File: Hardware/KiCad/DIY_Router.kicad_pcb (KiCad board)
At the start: 4 copper layers, 90 parts, among them IC1 HLK-7628N, IC2 TPS62A06ADRLR, J1 2171790001, J10 2041262-1, J2 RJ45_Hanrun_HR911105A_Horizon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, J3 RJ45_Hanrun_HR911105A_Horizon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, J4 RJ45_Hanrun_HR911105A_Horizon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, J5 Conn_01x06_Pin, J6 Conn_02x07_Odd_Even, J7 RJ45_Hanrun_HR911105A_Horizon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, J8 USB_A, J9 SIM8066-6-1-14-01-A, SW1 436333033816, SW2 436333033816, SW3 450405020524, U1 XR22801IL32TR-F, U2 USBLC6-2SC6Y, U3 USBLC6-2SC6Y, U4 USB2422T/MJ, U5 EMIF03-SIM02M8, Y1 ABM8-25.000MHZ-B2-T3, Y2 ABM8-24.000MHZ-B2-T

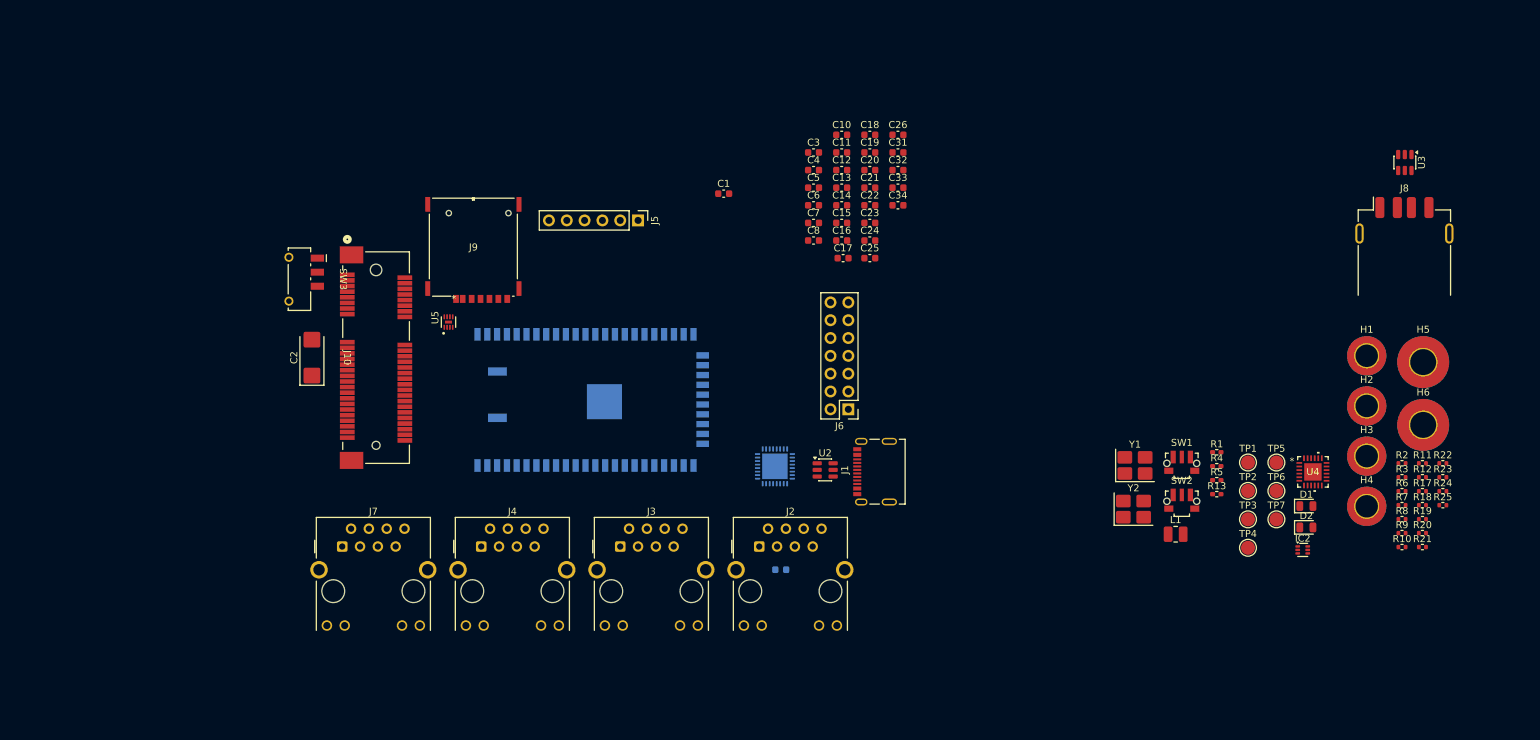
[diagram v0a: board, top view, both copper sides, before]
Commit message: Layout: Get started on PCB layout
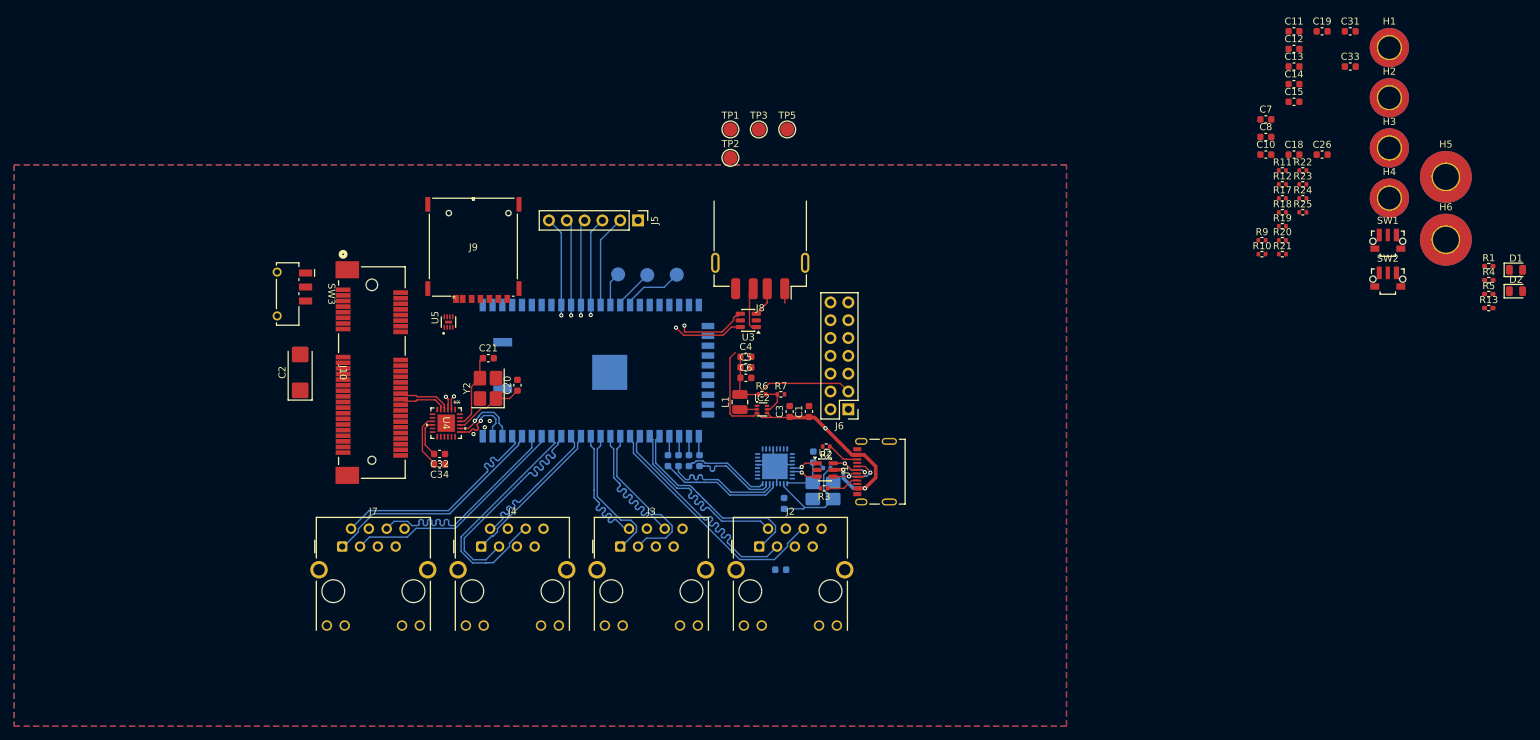
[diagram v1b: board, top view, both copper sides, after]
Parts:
- C16, C17, C22, C23, C24, C25, R8, TP4, TP6, TP7, Y1: moved to B.Cu
- moved U4 123.7 mm to (111.6, 86.8), turned to -90 degrees
- moved TP4 97.9 mm to (136.1, 65.6), turned to 180 degrees
- moved U3 96.2 mm to (154.7, 72.2), turned to 180 degrees
- moved TP6 94.8 mm to (140.2, 65.7), turned to 180 degrees
- moved Y2 93.6 mm to (117.5, 81.8), turned to 90 degrees
- moved TP7 92.3 mm to (144.4, 65.7), turned to 180 degrees
- moved R6 92.3 mm to (156.6, 82.7)
- moved J8 91.9 mm to (156.3, 60.4), turned to 180 degrees
- moved R7 89.9 mm to (159.3, 82.7)
- moved TP3 89.2 mm to (156.2, 45.0)
- moved TP1 87.7 mm to (152.1, 45.0)
- moved TP2 87.7 mm to (152.1, 49.0)
- moved TP5 84.3 mm to (160.2, 45.0)
- moved R3 82.4 mm to (165.4, 96.1), turned to 180 degrees
- moved R8 82.3 mm to (165.8, 93.2), turned to 180 degrees
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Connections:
- net MDI_RN_P0 renamed MDI_P0_RN
- net MDI_RN_P1 renamed MDI_P1_RN
- net MDI_RN_P2 renamed MDI_P2_RN
- net MDI_RN_P3 renamed MDI_P3_RN
- net MDI_RN_P4 renamed MDI_P4_RN
- net MDI_RP_P0 renamed MDI_P0_RP
- net MDI_RP_P1 renamed MDI_P1_RP
- net MDI_RP_P2 renamed MDI_P2_RP
- net MDI_RP_P3 renamed MDI_P3_RP
- net MDI_RP_P4 renamed MDI_P4_RP
- net MDI_TN_P0 renamed MDI_P0_TN
- net MDI_TN_P1 renamed MDI_P1_TN
- net MDI_TN_P2 renamed MDI_P2_TN
- net MDI_TN_P3 renamed MDI_P3_TN
- net MDI_TN_P4 renamed MDI_P4_TN
- net MDI_TP_P0 renamed MDI_P0_TP
- net MDI_TP_P1 renamed MDI_P1_TP
- net MDI_TP_P2 renamed MDI_P2_TP
- net MDI_TP_P3 renamed MDI_P3_TP
- net MDI_TP_P4 renamed MDI_P4_TP
- J1 pad A1B12: Net-(J1-CC2) -> GND
- J1 pad B1A12: Net-(J1-CC2) -> GND
- J1 pad SH1: Net-(J1-CC2) -> GND
- J1 pad SH2: Net-(J1-CC2) -> GND
- J1 pad SH3: Net-(J1-CC2) -> GND
- J1 pad SH4: Net-(J1-CC2) -> GND
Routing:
- net EPHY_LED4: track 0.00 -> 71.3 mm, vias 0 -> 1
- net EPHY_LED1: track 0.00 -> 68.5 mm, vias 0 -> 1
- net EPHY_LED3: track 0.00 -> 63.2 mm, vias 0 -> 1
- net EPHY_LED2: track 0.00 -> 60.4 mm, vias 0 -> 1
- net VBUS: track 0.00 -> 53.9 mm, vias 0 -> 3
- net /USB_HUB/USB_OUT_DN: track 0.00 -> 53.1 mm, vias 0 -> 2
- net /USB_HUB/USB_OUT_DP: track 0.00 -> 53.0 mm, vias 0 -> 2
- net MDI_P1_RN: track 0.00 -> 35.2 mm
- net MDI_P1_RP: track 0.00 -> 35.0 mm
- net MDI_P3_RN: track 0.00 -> 34.3 mm
- net MDI_P3_RP: track 0.00 -> 34.1 mm
- net MDI_P4_RP: track 0.00 -> 32.9 mm
- net MDI_P4_TP: track 0.00 -> 32.8 mm
- net MDI_P4_TN: track 0.00 -> 32.7 mm
- net MDI_P4_RN: track 0.00 -> 32.7 mm
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- added copper zone on B.Cu, net GND
- added copper zone on F.Cu, net GND
- added copper zone on In2.Cu, net GND

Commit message: Hardware: Lay out and route GPIO Header, USB and some other stuff
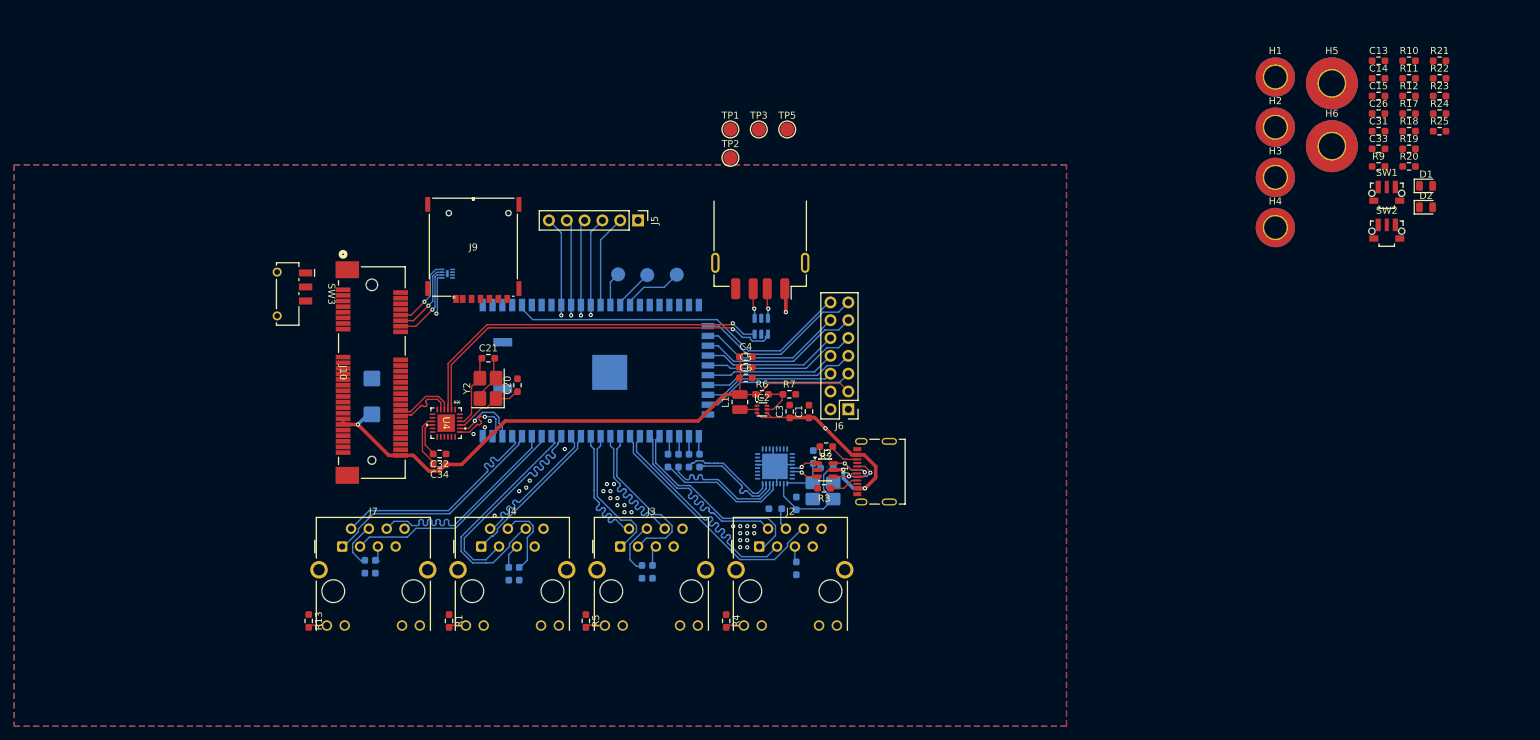
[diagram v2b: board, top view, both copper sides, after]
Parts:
- C1, C13, C14, C15, C16, C17, C20, C21, C22, C23, C24, C25, C26, C3, C31, C32, C33, C34, C4, C5, C6, C9: footprint Capacitor_SMD:C_0603_1608Metric -> Resistor_SMD:R_0603_1608Metric_Pad0.98x0.95mm_HandSolder
- C10, C11, C12, C18, C19, C7, C8: footprint Capacitor_SMD:C_0603_1608Metric -> Resistor_SMD:R_0603_1608Metric_Pad0.98x0.95mm_HandSolder; moved to B.Cu
- C2, U3, U5: moved to B.Cu
- R1, R13, R4, R5: footprint Resistor_SMD:R_0402_1005Metric_Pad0.72x0.64mm_HandSolder -> Resistor_SMD:R_0603_1608Metric_Pad0.98x0.95mm_HandSolder
- R10, R11, R12, R17, R18, R19, R2, R20, R21, R22, R23, R24, R25, R3, R6, R7, R8, R9: footprint Resistor_SMD:R_0402_1005Metric -> Resistor_SMD:R_0603_1608Metric_Pad0.98x0.95mm_HandSolder
- moved R13 174.0 mm to (92.0, 115.0), turned to -90 degrees
- moved R1 156.6 mm to (112.0, 115.0), turned to -90 degrees
- moved C19 155.0 mm to (101.5, 107.3), turned to -90 degrees
- moved C18 144.9 mm to (100.0, 107.3), turned to -90 degrees
- moved R5 136.9 mm to (131.5, 115.0), turned to -90 degrees
- moved C8 124.6 mm to (120.5, 108.3), turned to -90 degrees
- moved C7 124.6 mm to (122.0, 108.3), turned to -90 degrees
- moved C11 120.7 mm to (139.5, 108.0), turned to -90 degrees
- moved R4 119.0 mm to (151.5, 115.0), turned to -90 degrees
- moved C12 117.9 mm to (141.0, 108.0), turned to -90 degrees
- moved C10 89.2 mm to (161.5, 107.5), turned to -90 degrees
- moved R21 35.5 mm to (253.2, 35.2)
- moved R10 34.6 mm to (248.8, 35.2)
- moved R22 23.5 mm to (253.2, 37.7)
- moved R23 23.2 mm to (253.2, 40.2)
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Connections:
- J6 pad 11: /DIY_Router/I2C_SCL -> /DIY_Router/SPI_CS1
- J6 pad 12: /DIY_Router/SPI_CS1 -> /DIY_Router/I2C_SDA
- J6 pad 13: /DIY_Router/I2C_SDA -> /DIY_Router/I2C_SCL
- J6 pad 6: /DIY_Router/SPI_MOSI -> UART_TXD0
- J6 pad 7: UART_TXD0 -> /DIY_Router/GPIO0
- J6 pad 8: /DIY_Router/SPI_MISO -> /DIY_Router/SPI_MOSI
- J6 pad 9: /DIY_Router/GPIO0 -> /DIY_Router/SPI_MISO
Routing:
- net +3.3V: track 22.0 -> 89.2 mm, vias 0 -> 1
- net /DIY_Router/SPI_CS0: track 0.45 -> 49.9 mm
- net /DIY_Router/I2C_SCL: track 0.00 -> 24.7 mm
- net /DIY_Router/SPI_CS1: track 0.00 -> 23.4 mm
- net /DIY_Router/SPI_MISO: track 0.00 -> 22.0 mm
- net /DIY_Router/GPIO0: track 0.00 -> 21.7 mm
- net UART_RXD0: track 0.45 -> 21.8 mm
- net /DIY_Router/I2C_SDA: track 0.55 -> 21.5 mm
- net /DIY_Router/SPI_CLK: track 0.00 -> 19.6 mm
- net UART_TXD0: track 0.00 -> 18.7 mm
- net /DIY_Router/SPI_MOSI: track 0.31 -> 18.9 mm
- net /Mini_PCIe_SIM/USIM_RST: track 0.00 -> 11.4 mm, vias 0 -> 1
- net Net-(J4-TCT): track 0.00 -> 11.2 mm
- net /Mini_PCIe_SIM/USIM_CLK: track 0.00 -> 10.9 mm, vias 0 -> 1
- net /Mini_PCIe_SIM/USIM_DATA: track 0.00 -> 10.3 mm, vias 0 -> 1
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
